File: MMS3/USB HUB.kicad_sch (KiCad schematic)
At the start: 21 parts, among them U302 CH334P, Y900 Crystal_GND24

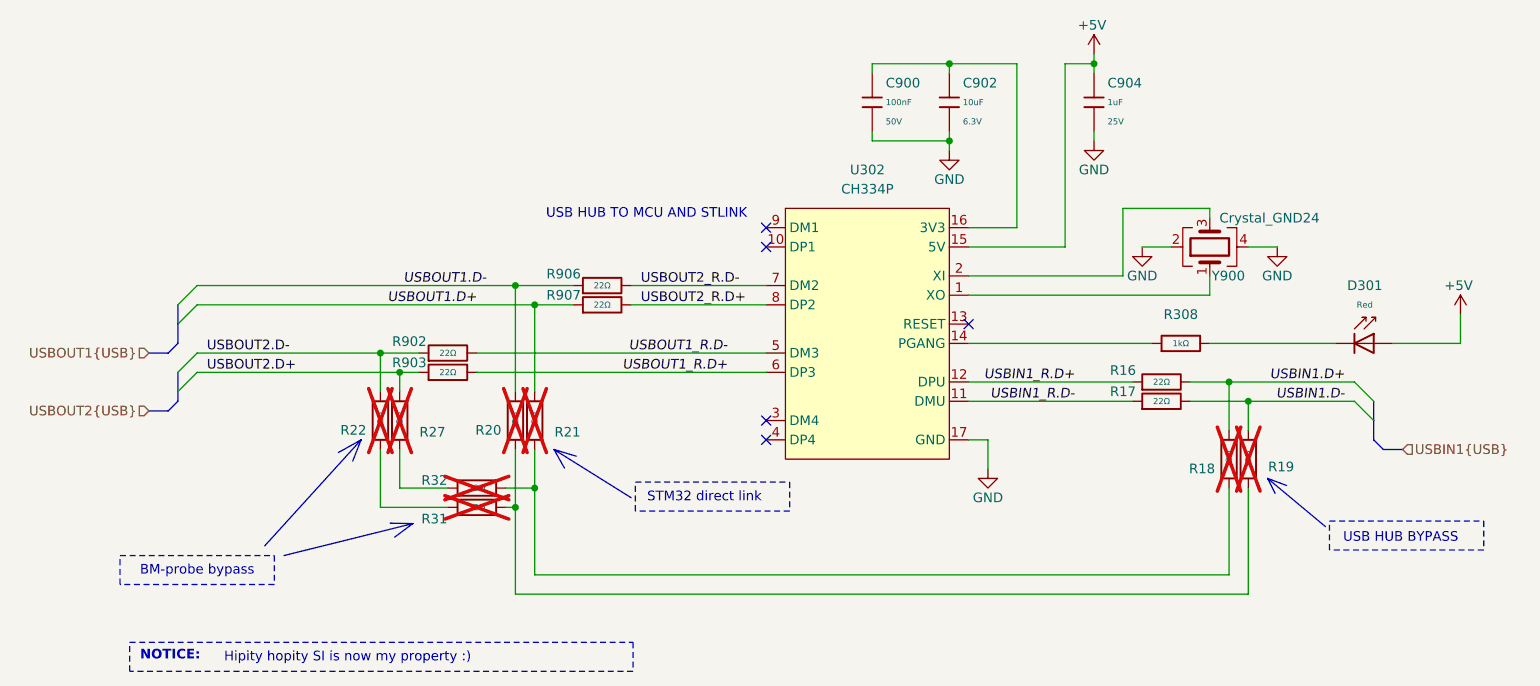
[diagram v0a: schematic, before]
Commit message: schematic + partly layout
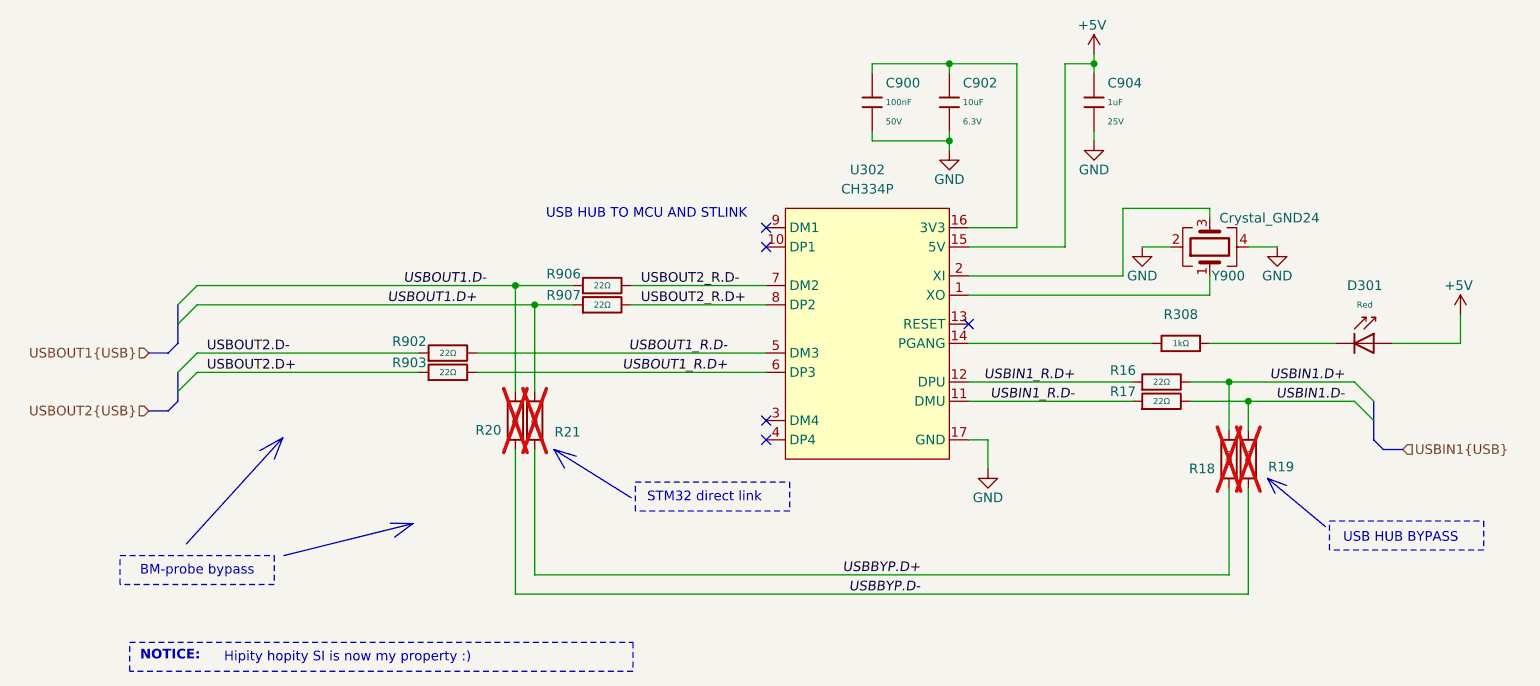
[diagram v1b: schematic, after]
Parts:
- removed R22, R27, R31, R32: 22Ω, PCM_JLCPCB:R_0402, symbol PCM_JLCPCB-Resistors:0402,22Ω
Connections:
- net USBBYP.D-: now reaches R19.1, R20.1
- net USBBYP.D+: now reaches R18.1, R21.1
